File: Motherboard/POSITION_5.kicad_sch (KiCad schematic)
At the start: 27 parts, among them Q20 MOSFET_N_(ZVN3320FTA), Q22 MOSFET_N_(DMN61D8LQ-13)

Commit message: Schematic ready.  Going to clean up directory now.
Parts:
- C26, C39, C40, C41, C42: footprint Capacitors_SMD:C_1206 -> Capacitor_SMD:C_1206_3216Metric
- CAL10, CAL9: footprint (none) -> Smart_Tank:FEMALE_SPADE_QC_(TE_63969-1)
- CTRL_SHUNT_5, PUMP_SHUNT_5: footprint _GARRETTS_PARTS:SHUNT_(WSL40261L000FEA) -> Smart_Tank:SHUNT_(WSL40261L000FEA)
- D12, D7: footprint Diodes_SMD:SOD-123 -> Diode_SMD:D_SMA
- Q20: footprint TO_SOT_Packages_SMD:SOT-23 -> Package_TO_SOT_SMD:SOT-23
- R11, R76, R79, R82, R83, R84: footprint Resistors_SMD:R_1206 -> Resistor_SMD:R_1206_3216Metric
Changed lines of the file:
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@@
 			)
 		)
-		(property "Footprint" ""
+		(property "Footprint" "Smart_Tank:FEMALE_SPADE_QC_(TE_63969-1)"
 			(at 254 31.75 0)
 			(effects
@@
 			)
 		)
-		(property "Footprint" "_GARRETTS_PARTS:SHUNT_(WSL40261L000FEA)"
+		(property "Footprint" "Smart_Tank:SHUNT_(WSL40261L000FEA)"
 			(at 195.58 52.578 90)
 			(effects
@@
 			)
 		)
-		(property "Footprint" "Capacitors_SMD:C_1206"
+		(property "Footprint" "Capacitor_SMD:C_1206_3216Metric"
 			(at 219.4052 138.43 0)
 			(effects
@@
 			)
 		)
-		(property "Footprint" ""
+		(property "Footprint" "Smart_Tank:FEMALE_SPADE_QC_(TE_63969-1)"
 			(at 195.58 106.68 0)
 			(effects
@@
 			)
 		)
-		(property "Footprint" "TO_SOT_Packages_SMD:SOT-23"
+		(property "Footprint" "Package_TO_SOT_SMD:SOT-23"
 			(at 119.38 93.345 0)
 			(effects
@@
 			)
 		)
-		(property "Footprint" "Resistors_SMD:R_1206"
+		(property "Footprint" "Resistor_SMD:R_1206_3216Metric"
 			(at 117.348 80.01 90)
 			(effects
@@
 			)
 		)
-		(property "Footprint" "Resistors_SMD:R_1206"
+		(property "Footprint" "Resistor_SMD:R_1206_3216Metric"
 			(at 190.5 76.962 90)
 			(effects
@@
 			)
 		)
-		(property "Footprint" "_GARRETTS_PARTS:SHUNT_(WSL40261L000FEA)"
+		(property "Footprint" "Smart_Tank:SHUNT_(WSL40261L000FEA)"
 			(at 195.58 138.938 90)
 			(effects
@@
 			)
 		)
-		(property "Footprint" "Diodes_SMD:SOD-123"
+		(property "Footprint" "Diode_SMD:D_SMA"
 			(at 254 40.64 0)
 			(effects
@@
 			)
 		)
-		(property "Footprint" "Capacitors_SMD:C_1206"
+		(property "Footprint" "Capacitor_SMD:C_1206_3216Metric"
 			(at 229.5652 52.07 0)
 			(effects
@@
 			)
 		)
-		(property "Footprint" "Diodes_SMD:SOD-123"
+		(property "Footprint" "Diode_SMD:D_SMA"
 			(at 237.49 78.74 0)
 			(effects
@@
 			)
 		)
-		(property "Footprint" "Resistors_SMD:R_1206"
+		(property "Footprint" "Resistor_SMD:R_1206_3216Metric"
 			(at 101.6 90.932 90)
 			(effects
@@
 			)
 		)
-		(property "Footprint" "Capacitors_SMD:C_1206"
+		(property "Footprint" "Capacitor_SMD:C_1206_3216Metric"
 			(at 219.4052 52.07 0)
 			(effects
@@
 			)
 		)
-		(property "Footprint" "Capacitors_SMD:C_1206"
+		(property "Footprint" "Capacitor_SMD:C_1206_3216Metric"
 			(at 229.5652 138.43 0)
 			(effects
@@
 			)
 		)
-		(property "Footprint" "Resistors_SMD:R_1206"
+		(property "Footprint" "Resistor_SMD:R_1206_3216Metric"
 			(at 94.488 97.79 90)
 			(effects
@@
 			)
 		)
-		(property "Footprint" "Resistors_SMD:R_1206"
+		(property "Footprint" "Resistor_SMD:R_1206_3216Metric"
 			(at 185.928 85.09 90)
 			(effects
@@
 			)
 		)
-		(property "Footprint" "Capacitors_SMD:C_1206"
+		(property "Footprint" "Capacitor_SMD:C_1206_3216Metric"
 			(at 257.81 47.2948 0)
 			(effects
@@
 			)
 		)
-		(property "Footprint" "Resistors_SMD:R_1206"
+		(property "Footprint" "Resistor_SMD:R_1206_3216Metric"
 			(at 74.168 41.91 90)
 			(effects

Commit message: Started cleaning out old parts from PCB.
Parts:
- PUMP_V_CONN_5: footprint Smart_Tank:PHNX_TB_SCREW_4_POS_(1729144) -> Smart_Tank:PHX_TB_HDR_4_POS_STR_(1755752)
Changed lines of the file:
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@@
 			)
 		)
-		(property "Footprint" "Smart_Tank:PHNX_TB_SCREW_4_POS_(1729144)"
+		(property "Footprint" "Smart_Tank:PHX_TB_HDR_4_POS_STR_(1755752)"
 			(at 250.19 82.55 0)
 			(effects

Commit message: Almost done with re-routing.
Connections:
- net POS_5_SPARE renamed POS_5_SPR_1
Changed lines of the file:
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@@
 		)
 	)
-	(global_label "POS_5_SPARE"
+	(global_label "POS_5_SPR_1"
 		(shape input)
 		(at 58.42 58.42 0)

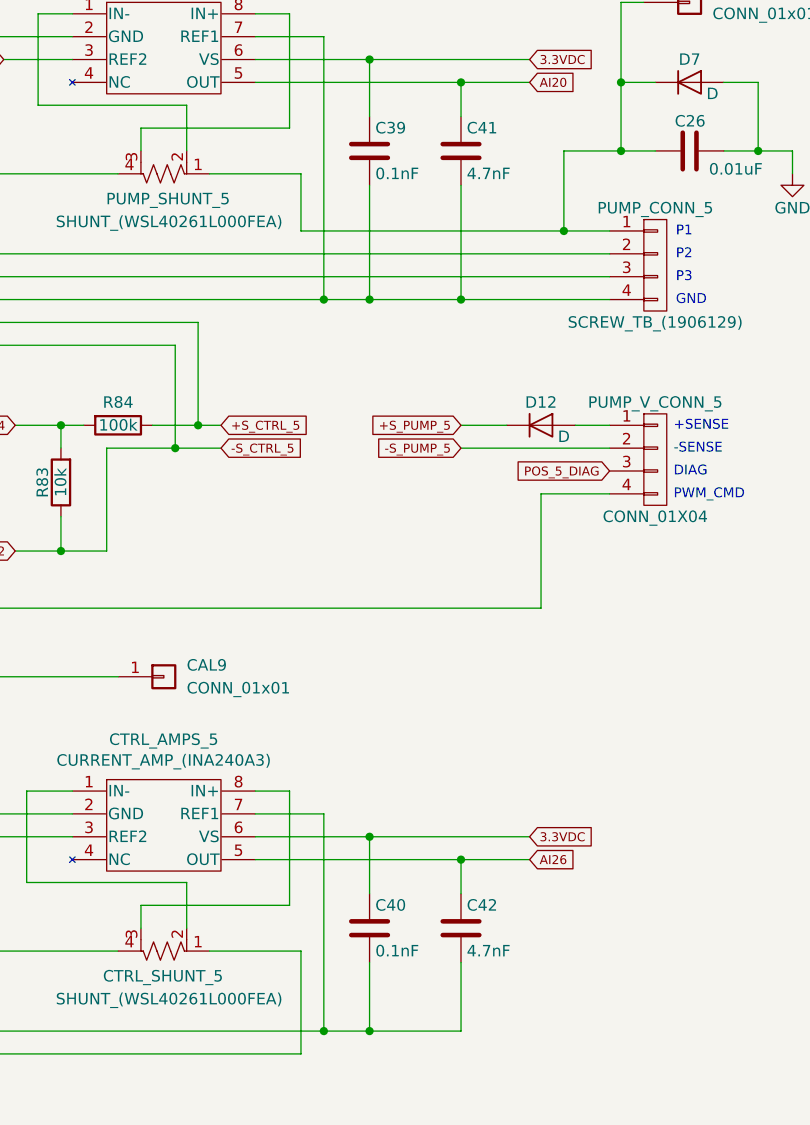
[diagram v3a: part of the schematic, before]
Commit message: Capacitor part issues...
Made these changes...

Concerning C13, C15, C27, C28, C31, C32, C35, C36, C39, C40, C43, C44
The schematic is wrong, and the BOM is correct.  These should all be 0.1uF
Concerning C20, C21, C29, C30, C33, C34, C37, C38, C41, C42, C45, C46
The BOM is wrong, and the schematic is correct.  These should all be 4.7nF
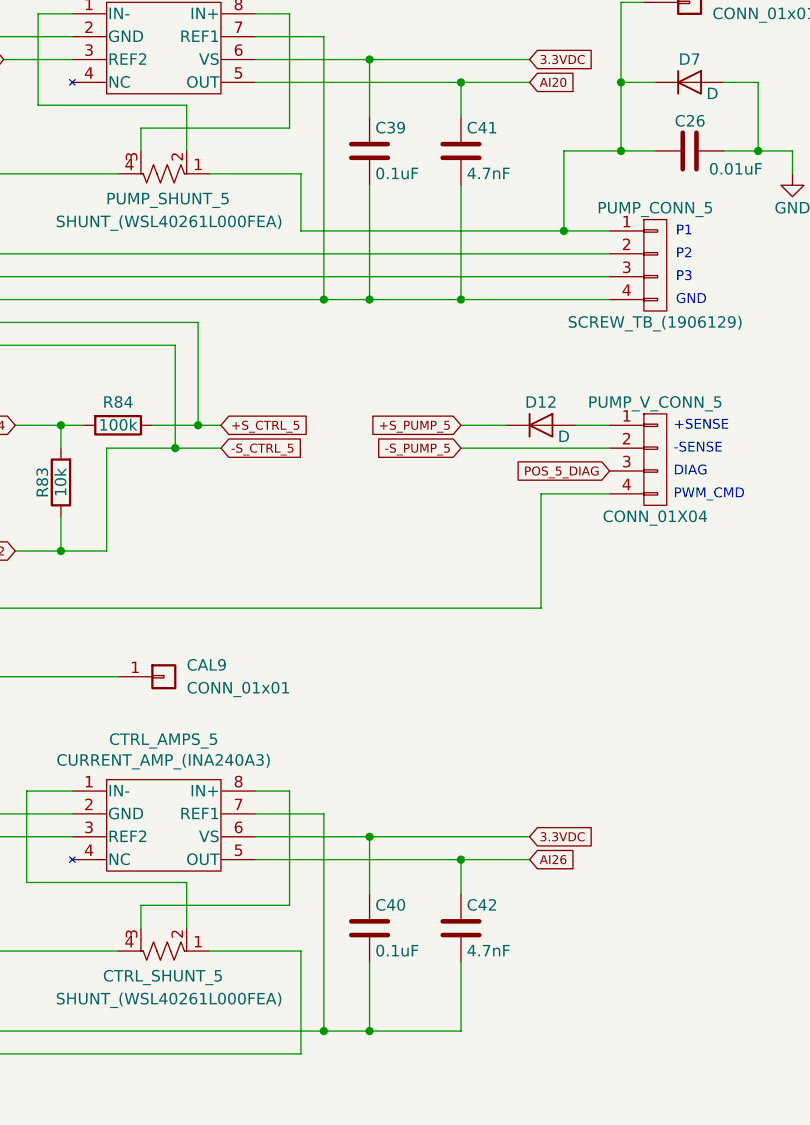
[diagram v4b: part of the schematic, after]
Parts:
- C39, C40: value 0.1nF -> 0.1uF
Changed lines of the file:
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@@
 			)
 		)
-		(property "Value" "0.1nF"
+		(property "Value" "0.1uF"
 			(at 219.075 137.16 0)
 			(effects
@@
 			)
 		)
-		(property "Value" "0.1nF"
+		(property "Value" "0.1uF"
 			(at 219.075 50.8 0)
 			(effects
